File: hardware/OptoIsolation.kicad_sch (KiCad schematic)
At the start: 20 parts

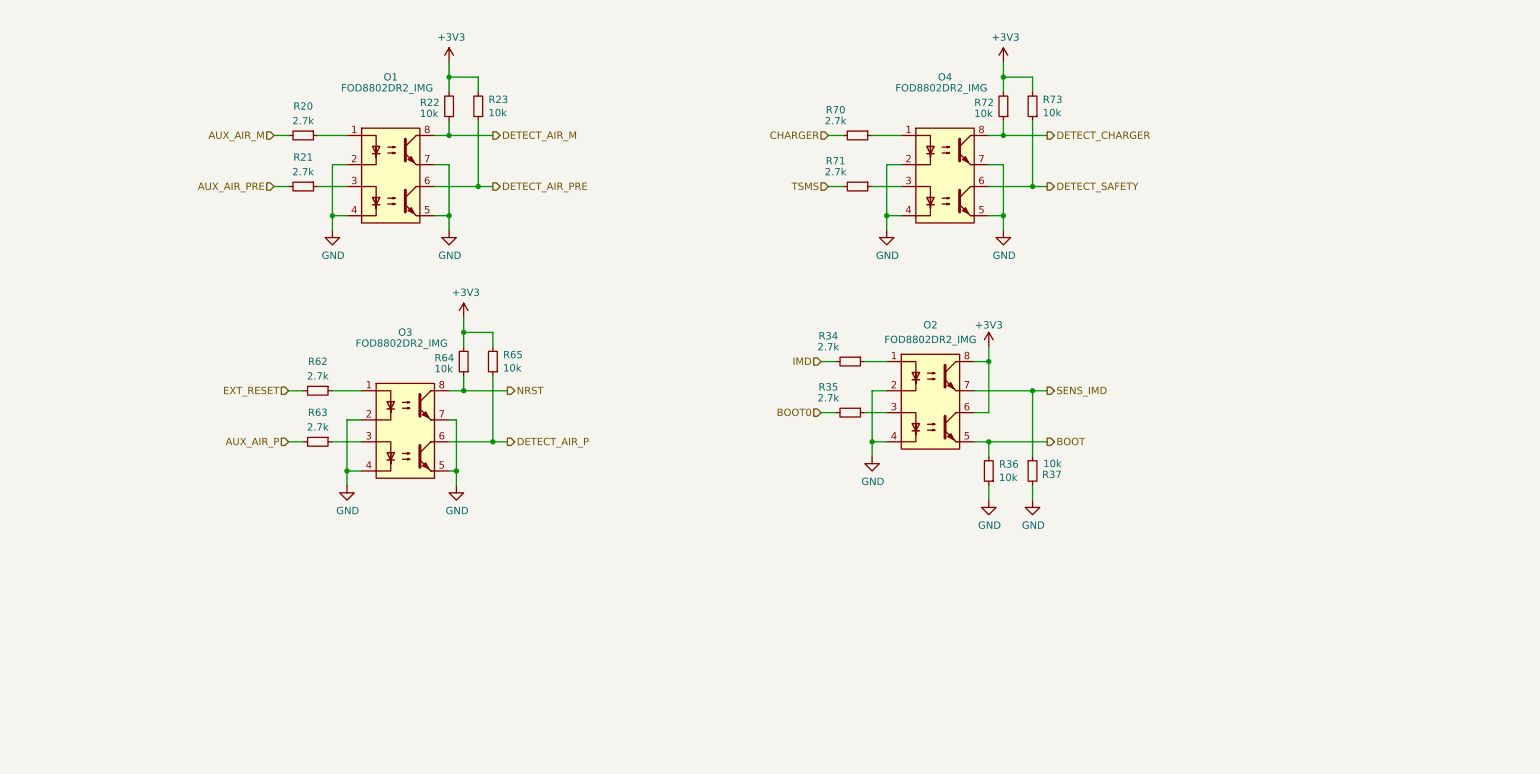
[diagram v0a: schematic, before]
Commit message: fixed some footprints; shorted pcb board to 60x100; re-designed the HV & current measuring as well as LTC communication, all are in one TS section;
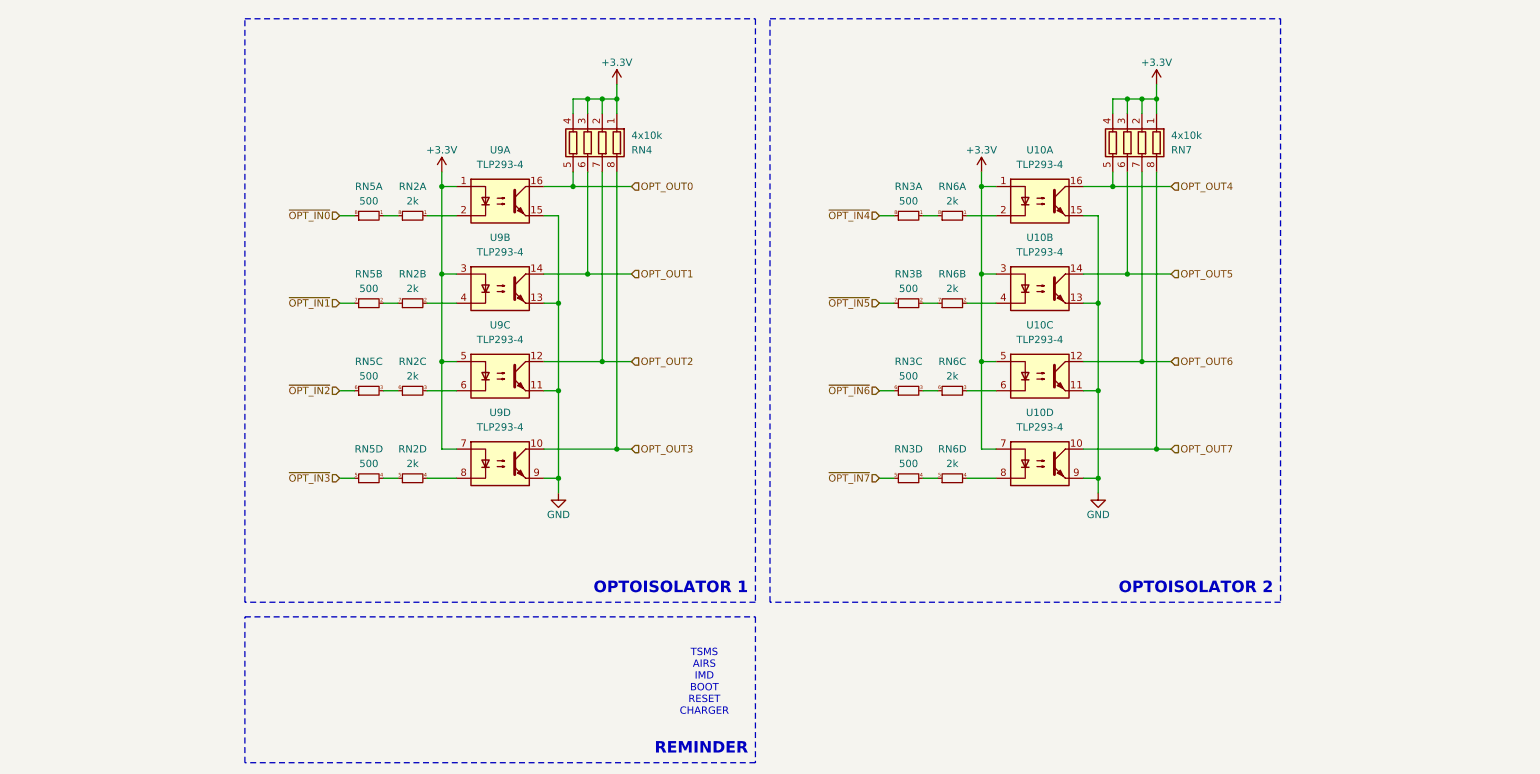
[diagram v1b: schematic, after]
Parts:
- removed O1, O2, O3, O4: FOD8802DR2_IMG, Opto 2 ch:SOIC127P600X175-8N, symbol Opto 2 ch:FOD8802DR2_IMG
- removed R20, R21, R34, R35, R62, R63, R70, R71: 2.7k, Resistor_SMD:R_0603_1608Metric, symbol Device:R_Small
- removed R22, R23, R36, R37, R64, R65, R72, R73: 10k, Resistor_SMD:R_0603_1608Metric, symbol Device:R_Small
- added RN2, RN6: 2k, Resistor_SMD:R_Array_Convex_4x0603, symbol Device:R_Pack04_Split
- added RN3, RN5: 500, Resistor_SMD:R_Array_Convex_4x0603, symbol Device:R_Pack04_Split
- added RN4, RN7: 4x10k, Resistor_SMD:R_Array_Convex_4x0603, symbol Device:R_Pack04
- added U10, U9: TLP293-4, Package_SO:SOIC-16_4.55x10.3mm_P1.27mm, symbol Isolator:TLP293-4
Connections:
- net GND: now also U10.11, U10.13, U10.15, U10.9, U9.11, U9.13, U9.15, U9.9
- new net: RN2.1 (R1.1), U9.2
- new net: RN2.8 (R1.2), RN5.1 (R1.1)
- new net: RN6.1 (R1.1), U10.2
- new net: RN6.3 (R3.1), U10.6
- new net: RN2.3 (R3.1), U9.6
- new net: RN2.6 (R3.2), RN5.3 (R3.1)
- new net: RN6.4 (R4.1), U10.8
- new net: RN3.4 (R4.1), RN6.5 (R4.2)
- new net: RN6.2 (R2.1), U10.4
- new net: RN3.2 (R2.1), RN6.7 (R2.2)
- new net: RN3.1 (R1.1), RN6.8 (R1.2)
- new net: RN2.2 (R2.1), U9.4
- new net: RN2.7 (R2.2), RN5.2 (R2.1)
- new net: RN2.4 (R4.1), U9.8
- new net: RN2.5 (R4.2), RN5.4 (R4.1)
- new net: RN3.3 (R3.1), RN6.6 (R3.2)
- new net +3.3V: RN4.1 (R1.1), RN4.2 (R2.1), RN4.3 (R3.1), RN4.4 (R4.1), RN7.1 (R1.1), RN7.2 (R2.1), RN7.3 (R3.1), RN7.4 (R4.1), U10.1, U10.3, U10.5, U10.7, U9.1, U9.3, U9.5, U9.7
- new net OPT_OUT0: RN4.5 (R4.2), U9.16
- new net OPT_OUT1: RN4.6 (R3.2), U9.14
- new net OPT_OUT2: RN4.7 (R2.2), U9.12
- new net OPT_OUT3: RN4.8 (R1.2), U9.10
- new net OPT_OUT4: RN7.5 (R4.2), U10.16
- new net OPT_OUT5: RN7.6 (R3.2), U10.14
- new net OPT_OUT6: RN7.7 (R2.2), U10.12
- new net OPT_OUT7: RN7.8 (R1.2), U10.10
- new net ~{OPT_IN0}: RN5.8 (R1.2)
- new net ~{OPT_IN1}: RN5.7 (R2.2)
- new net ~{OPT_IN2}: RN5.6 (R3.2)
- new net ~{OPT_IN3}: RN5.5 (R4.2)
- new net ~{OPT_IN4}: RN3.8 (R1.2)
- new net ~{OPT_IN5}: RN3.7 (R2.2)
- new net ~{OPT_IN6}: RN3.6 (R3.2)
- new net ~{OPT_IN7}: RN3.5 (R4.2)
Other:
- note added: "OPTOISOLATOR 1"
- note added: "OPTOISOLATOR 2"
- note added: "REMINDER"
- note added: "TSMS AIRS IMD BOOT RESET CHARGER"

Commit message: changes tbc
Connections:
- net +3.3V: no longer U9.1, U9.3, U9.5, U9.7
- net GND: now also U9.2, U9.4, U9.6, U9.8
- net at RN2.1 (R1.1): now also U9.1; no longer U9.2
- net at RN2.3 (R3.1): now also U9.5; no longer U9.6
- net at RN2.2 (R2.1): now also U9.3; no longer U9.4
- net at RN2.4 (R4.1): now also U9.7; no longer U9.8
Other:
- moved on the sheet: RN2A, RN2B, RN2C, RN2D, RN5A, RN5B, RN5C, RN5D

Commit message: sync
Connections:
- net +3.3V: no longer U10.1, U10.3, U10.5, U10.7
- net GND: now also U10.2, U10.4, U10.6, U10.8
- net at RN6.1 (R1.1): now also U10.1; no longer U10.2
- net at RN6.3 (R3.1): now also U10.5; no longer U10.6
- net at RN6.4 (R4.1): now also U10.7; no longer U10.8
- net at RN6.2 (R2.1): now also U10.3; no longer U10.4
- net OPT_OUT0 renamed ~{OPT_OUT1}
- net OPT_OUT1 renamed ~{OPT_OUT2}
- net OPT_OUT2 renamed ~{OPT_OUT3}
- net OPT_OUT3 renamed ~{OPT_OUT4}
- net OPT_OUT4 renamed ~{OPT_OUT5}
- net OPT_OUT5 renamed ~{OPT_OUT6}
- net OPT_OUT6 renamed ~{OPT_OUT7}
- net OPT_OUT7 renamed ~{OPT_OUT8}
- net ~{OPT_IN0} renamed OPT_IN1
- net ~{OPT_IN1} renamed OPT_IN2
- net ~{OPT_IN2} renamed OPT_IN3
- net ~{OPT_IN3} renamed OPT_IN4
- net ~{OPT_IN4} renamed OPT_IN5
- net ~{OPT_IN5} renamed OPT_IN6
- net ~{OPT_IN6} renamed OPT_IN7
- net ~{OPT_IN7} renamed OPT_IN8
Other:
- moved on the sheet: RN3A, RN3B, RN3C, RN3D, RN6A, RN6B, RN6C, RN6D

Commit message: sync
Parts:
- removed RN2: 2k, Resistor_SMD:R_Array_Convex_4x0603, symbol Device:R_Pack04_Split
- removed RN5: 500, Resistor_SMD:R_Array_Convex_4x0603, symbol Device:R_Pack04_Split
- removed U10: TLP293-4, Package_SO:SOIC-16_4.55x10.3mm_P1.27mm, symbol Isolator:TLP293-4
- added D11, D13: ESDA5V3SC5, Package_TO_SOT_SMD:SOT-23-6, symbol Power_Protection:ESDA5V3SC5
- added Q14, Q15, Q16, Q17, Q18, Q19, Q20, Q21: 2N7002, Package_TO_SOT_SMD:SOT-23, symbol Transistor_FET:2N7002
- added RN14, RN2: 4x200, Resistor_SMD:R_Array_Convex_4x0603, symbol Device:R_Pack04
- added RN15: 4x10k, Resistor_SMD:R_Array_Convex_4x0603, symbol Device:R_Pack04
- added RN5: 4x1M, Resistor_SMD:R_Array_Convex_4x0603, symbol Device:R_Pack04
- added U5: TLP293-4, Package_SO:SOIC-16_4.55x10.3mm_P1.27mm, symbol Isolator:TLP293-4
- RN3: value 500 -> 100
- RN6: value 2k -> 100
- RN7: value 4x10k -> 4x1M
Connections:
- net +3.3V: now also RN14.1 (R1.1), RN14.2 (R2.1), RN14.3 (R3.1), RN14.4 (R4.1), RN15.1 (R1.1), RN15.2 (R2.1), RN15.3 (R3.1), RN15.4 (R4.1), RN2.1 (R1.1), RN2.2 (R2.1), RN2.3 (R3.1), RN2.4 (R4.1); no longer RN7.1 (R1.1), RN7.2 (R2.1), RN7.3 (R3.1), RN7.4 (R4.1)
- net GND: now also RN7.5 (R4.2), RN7.6 (R3.2), RN7.7 (R2.2), RN7.8 (R1.2), D11.2 (K), D11.5 (NC), D13.2 (K), D13.5 (NC), Q14.2 (S), Q15.2 (S), Q16.2 (S), Q17.2 (S), Q18.2 (S), Q19.2 (S), Q20.2 (S), Q21.2 (S), RN5.5 (R4.2), RN5.6 (R3.2), RN5.7 (R2.2), RN5.8 (R1.2), U5.11, U5.13, U5.15, U5.9; no longer U9.2, U9.4, U9.6, U9.8
- net OPT_IN1: now also RN3.8 (R1.2)
- net OPT_IN2: now also RN3.7 (R2.2)
- net OPT_IN3: now also RN3.6 (R3.2)
- net OPT_IN4: now also RN3.5 (R4.2)
- net OPT_IN5: now also RN6.8 (R1.2); no longer RN3.8 (R1.2)
- net OPT_IN6: now also RN6.7 (R2.2); no longer RN3.7 (R2.2)
- net OPT_IN7: now also RN6.6 (R3.2); no longer RN3.6 (R3.2)
- net OPT_IN8: now also RN6.5 (R4.2); no longer RN3.5 (R4.2)
- net ~{OPT_OUT5}: now also RN15.5 (R4.2), U5.16; no longer RN7.5 (R4.2)
- net ~{OPT_OUT6}: now also RN15.6 (R3.2), U5.14; no longer RN7.6 (R3.2)
- net ~{OPT_OUT7}: now also RN15.7 (R2.2), U5.12; no longer RN7.7 (R2.2)
- net ~{OPT_OUT8}: now also RN15.8 (R1.2), U5.10; no longer RN7.8 (R1.2)
- net at U9.1: now also RN2.8 (R1.2)
- net at RN6.1 (R1.1): now also RN7.4 (R4.1), D13.1 (A), Q18.1 (G)
- net at RN6.3 (R3.1): now also RN7.2 (R2.1), D13.4 (A), Q20.1 (G)
- net at U9.5: now also RN2.6 (R3.2)
- net at RN6.4 (R4.1): now also RN7.1 (R1.1), D13.6 (A), Q21.1 (G)
- net at RN3.4 (R4.1): now also D11.6 (A), Q17.1 (G), RN5.1 (R1.1); no longer RN6.5 (R4.2)
- net at RN6.2 (R2.1): now also RN7.3 (R3.1), D13.3 (A), Q19.1 (G)
- net at RN3.2 (R2.1): now also D11.3 (A), Q15.1 (G), RN5.3 (R3.1); no longer RN6.7 (R2.2)
- net at RN3.1 (R1.1): now also D11.1 (A), Q14.1 (G), RN5.4 (R4.1); no longer RN6.8 (R1.2)
- net at U9.3: now also RN2.7 (R2.2)
- net at U9.7: now also RN2.5 (R4.2)
- net at RN3.3 (R3.1): now also D11.4 (A), Q16.1 (G), RN5.2 (R2.1); no longer RN6.6 (R3.2)
- new net: Q19.3 (D), U5.4
- new net: Q16.3 (D), U9.6
- new net: Q20.3 (D), U5.6
- new net: Q15.3 (D), U9.4
- new net: RN14.5 (R4.2), U5.7
- new net: Q21.3 (D), U5.8
- new net: RN14.7 (R2.2), U5.3
- new net: Q14.3 (D), U9.2
- new net: RN14.8 (R1.2), U5.1
- new net: Q18.3 (D), U5.2
- new net: RN14.6 (R3.2), U5.5
- new net: Q17.3 (D), U9.8
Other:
- note removed: "OPTOISOLATOR 2"
- moved on the sheet: RN4, U9A, U9B, U9C, U9D

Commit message: schematic done
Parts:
- removed D11, D13: ESDA5V3SC5, Package_TO_SOT_SMD:SOT-23-6, symbol Power_Protection:ESDA5V3SC5
- removed Q14, Q15, Q16, Q17, Q18, Q19, Q20, Q21: 2N7002, Package_TO_SOT_SMD:SOT-23, symbol Transistor_FET:2N7002
- removed RN14, RN2: 4x200, Resistor_SMD:R_Array_Convex_4x0603, symbol Device:R_Pack04
- removed RN15, RN4: 4x10k, Resistor_SMD:R_Array_Convex_4x0603, symbol Device:R_Pack04
- removed RN3, RN6: 100, Resistor_SMD:R_Array_Convex_4x0603, symbol Device:R_Pack04_Split
- removed RN5, RN7: 4x1M, Resistor_SMD:R_Array_Convex_4x0603, symbol Device:R_Pack04
- removed U5, U9: TLP293-4, Package_SO:SOIC-16_4.55x10.3mm_P1.27mm, symbol Isolator:TLP293-4
